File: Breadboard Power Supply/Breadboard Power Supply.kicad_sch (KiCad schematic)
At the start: 17 parts, among them J1 Conn_01x02_Pin, J2 Conn_01x02_Pin, J3 Conn_01x03_Pin, J4 Conn_01x03_Pin, J5 Screw_Terminal_01x02, J6 Screw_Terminal_01x02, J7 Barrel_Jack_Switch, U1 LM7805_TO220, U2 LM317_TO-220

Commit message: Add power input/output net classes and update schematic labels for clarity
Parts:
- D1: Purpose (none) -> Power
- J1, J2: Purpose (none) -> Output to breadboard
- J3: Purpose (none) -> Output voltage selector 1
- J4: Purpose (none) -> Output voltage selector 2
- J5, J6: Purpose (none) -> Output to jumper wires
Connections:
- net PWR_output: now reaches J1.2 (Pin_2), J3.2 (Pin_2), J5.2 (Pin_2)
- net PWR_output: now also J2.2 (Pin_2), J4.2 (Pin_2), J6.2 (Pin_2)
- net PWR_input: now reaches J7.1, S1.2
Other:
- note added: "3.3V circuit"
- note added: "GND (Pin 1)"
- note added: "Input and 5V circuit"
- note added: "Output and switches"
- moved on the sheet: J3, J4
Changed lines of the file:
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@@
 		(rev "1")
+	)
+	(rectangle
+		(start 40.64 91.44)
+		(end 151.13 145.415)
+		(stroke
+			(width 0)
+			(type default)
+		)
+		(fill
+			(type none)
+		)
+	)
+	(rectangle
+		(start 179.705 47.625)
+		(end 244.475 155.575)
+		(stroke
+			(width 0)
+			(type default)
+		)
+		(fill
+			(type none)
+		)
+	)
+	(rectangle
+		(start 26.035 27.305)
+		(end 151.13 78.74)
+		(stroke
+			(width 0)
+			(type default)
+		)
+		(fill
+			(type none)
+		)
+	)
+	(text "3.3V circuit"
+		(exclude_from_sim no)
+		(at 46.99 88.9 0)
+		(effects
+			(font
+				(size 1.27 1.27)
+			)
+		)
+	)
+	(text "GND (Pin 1)"
+		(exclude_from_sim no)
+		(at 210.82 137.16 0)
+		(effects
+			(font
+				(size 1.27 1.27)
+			)
+		)
+	)
+	(text "Output and switches"
+		(exclude_from_sim no)
+		(at 189.23 44.45 0)
+		(effects
+			(font
+				(size 1.27 1.27)
+			)
+		)
+	)
+	(text "GND (Pin 1)"
+		(exclude_from_sim no)
+		(at 210.82 81.28 0)
+		(effects
+			(font
+				(size 1.27 1.27)
+			)
+		)
+	)
+	(text "Input and 5V circuit"
+		(exclude_from_sim no)
+		(at 35.56 25.4 0)
+		(effects
+			(font
+				(size 1.27 1.27)
+			)
+		)
 	)
 	(junction
@@
 	(wire
 		(pts
-			(xy 201.93 60.96) (xy 201.93 68.58)
+			(xy 201.93 58.42) (xy 201.93 68.58)
 		)
 		(stroke
@@
 	(wire
 		(pts
-			(xy 208.28 116.84) (xy 201.93 116.84)
+			(xy 208.28 114.3) (xy 201.93 114.3)
 		)
 		(stroke
@@
 	(wire
 		(pts
-			(xy 208.28 60.96) (xy 201.93 60.96)
+			(xy 208.28 58.42) (xy 201.93 58.42)
 		)
 		(stroke
@@
 	(wire
 		(pts
-			(xy 201.93 116.84) (xy 201.93 124.46)
+			(xy 201.93 114.3) (xy 201.93 124.46)
 		)
 		(stroke
@@
 		)
 	)
+	(label "PWR_output"
+		(at 201.93 121.92 180)
+		(effects
+			(font
+				(size 1.27 1.27)
+			)
+			(justify right bottom)
+		)
+	)
 	(label "12V"
 		(at 57.15 101.6 0)
@@
 	)
 	(label "5V"
-		(at 208.28 58.42 180)
+		(at 208.28 55.88 180)
 		(effects
 			(font
@@
 		)
 	)
+	(label "PWR_output"
+		(at 201.93 66.04 180)
+		(effects
+			(font
+				(size 1.27 1.27)
+			)
+			(justify right bottom)
+		)
+	)
 	(label "3.3V"
-		(at 208.28 63.5 180)
+		(at 208.28 60.96 180)
 		(effects
 			(font
@@
 	)
 	(label "5V"
-		(at 208.28 114.3 180)
+		(at 208.28 111.76 180)
 		(effects
 			(font
@@
 		)
 	)
+	(label "PWR_input"
+		(at 53.34 45.72 0)
+		(effects
+			(font
+				(size 1.27 1.27)
+			)
+			(justify left bottom)
+		)
+	)
 	(label "3.3V"
-		(at 208.28 119.38 180)
+		(at 208.28 116.84 180)
 		(effects
 			(font
@@
 		)
 		(property "Value" "Screw_Terminal_01x02"
-			(at 213.36 76.2001 0)
+			(at 203.2 73.66 0)
 			(effects
 				(font
@@
 				)
 				(hide yes)
+			)
+		)
+		(property "Purpose" "Output to jumper wires"
+			(at 224.79 76.2 0)
+			(effects
+				(font
+					(size 1.27 1.27)
+				)
 			)
 		)
@@
 		(on_board yes)
 		(dnp no)
-		(fields_autoplaced yes)
 		(property "Reference" "J2"
 			(at 214.63 124.4599 0)
@@
 				)
 				(hide yes)
+			)
+		)
+		(property "Purpose" "Output to breadboard"
+			(at 213.36 121.92 0)
+			(effects
+				(font
+					(size 1.27 1.27)
+				)
 			)
 		)
@@
 		(on_board yes)
 		(dnp no)
-		(fields_autoplaced yes)
 		(property "Reference" "J1"
 			(at 214.63 68.5799 0)
@@
 				)
 				(hide yes)
+			)
+		)
+		(property "Purpose" "Output to breadboard"
+			(at 213.36 66.04 0)
+			(effects
+				(font
+					(size 1.27 1.27)
+				)
 			)
 		)
@@
 	(symbol
 		(lib_id "Connector:Conn_01x03_Pin")
-		(at 213.36 60.96 180)
+		(at 213.36 58.42 180)
 		(unit 1)
 		(exclude_from_sim no)
@@
 		(on_board yes)
 		(dnp no)
-		(fields_autoplaced yes)
 		(property "Reference" "J3"
+			(at 214.63 57.1499 0)
+			(effects
+				(font
+					(size 1.27 1.27)
+				)
+				(justify right)
+			)
+		)
+		(property "Value" "Conn_01x03_Pin"
 			(at 214.63 59.6899 0)
 			(effects
@@
 			)
 		)
-		(property "Value" "Conn_01x03_Pin"
-			(at 214.63 62.2299 0)
-			(effects
-				(font
-					(size 1.27 1.27)
-				)
-				(justify right)
-			)
-		)
 		(property "Footprint" "Connector_PinHeader_2.54mm:PinHeader_1x03_P2.54mm_Vertical"
-			(at 213.36 60.96 0)
+			(at 213.36 58.42 0)
 			(effects
 				(font
@@
 		)
 		(property "Datasheet" "~"
-			(at 213.36 60.96 0)
+			(at 213.36 58.42 0)
 			(effects
 				(font
@@
 		)
 		(property "Description" "Generic connector, single row, 01x03, script generated"
-			(at 213.36 60.96 0)
-			(effects
-				(font
-					(size 1.27 1.27)
-				)
-				(hide yes)
+			(at 213.36 58.42 0)
+			(effects
+				(font
+					(size 1.27 1.27)
+				)
+				(hide yes)
+			)
+		)
+		(property "Purpose" "Output voltage selector 1"
+			(at 213.36 52.07 0)
+			(effects
+				(font
+					(size 1.27 1.27)
+				)
 			)
 		)
@@
 	(symbol
 		(lib_id "Connector:Conn_01x03_Pin")
-		(at 213.36 116.84 180)
+		(at 213.36 114.3 180)
 		(unit 1)
 		(exclude_from_sim no)
@@
 		(on_board yes)
 		(dnp no)
-		(fields_autoplaced yes)
 		(property "Reference" "J4"
+			(at 214.63 113.0299 0)
+			(effects
+				(font
+					(size 1.27 1.27)
+				)
+				(justify right)
+			)
+		)
+		(property "Value" "Conn_01x03_Pin"
 			(at 214.63 115.5699 0)
 			(effects
@@
 			)
 		)
-		(property "Value" "Conn_01x03_Pin"
-			(at 214.63 118.1099 0)
-			(effects
-				(font
-					(size 1.27 1.27)
-				)
-				(justify right)
-			)
-		)
 		(property "Footprint" "Connector_PinHeader_2.54mm:PinHeader_1x03_P2.54mm_Vertical"
-			(at 213.36 116.84 0)
+			(at 213.36 114.3 0)
 			(effects
 				(font
@@
 		)
 		(property "Datasheet" "~"
-			(at 213.36 116.84 0)
+			(at 213.36 114.3 0)
 			(effects
 				(font
@@
 		)
 		(property "Description" "Generic connector, single row, 01x03, script generated"
-			(at 213.36 116.84 0)
-			(effects
-				(font
-					(size 1.27 1.27)
-				)
-				(hide yes)
+			(at 213.36 114.3 0)
+			(effects
+				(font
+					(size 1.27 1.27)
+				)
+				(hide yes)
+			)
+		)
+		(property "Purpose" "Output voltage selector 2"
+			(at 213.36 107.95 0)
+			(effects
+				(font
+					(size 1.27 1.27)
+				)
 			)
 		)
@@
 		)
 		(property "Value" "Screw_Terminal_01x02"
-			(at 213.36 132.0801 0)
+			(at 203.2 129.54 0)
 			(effects
 				(font
@@
 				)
 				(hide yes)
+			)
+		)
+		(property "Purpose" "Output to jumper wires"
+			(at 224.79 132.08 0)
+			(effects
+				(font
+					(size 1.27 1.27)
+				)
 			)
 		)
@@
 		(on_board yes)
 		(dnp no)
-		(fields_autoplaced yes)
 		(property "Reference" "D1"
 			(at 77.7875 127 0)
@@
 			)
 		)
+		(property "Purpose" "Power"
+			(at 76.2 137.16 0)
+			(effects
+				(font
+					(size 1.27 1.27)
+				)
+			)
+		)

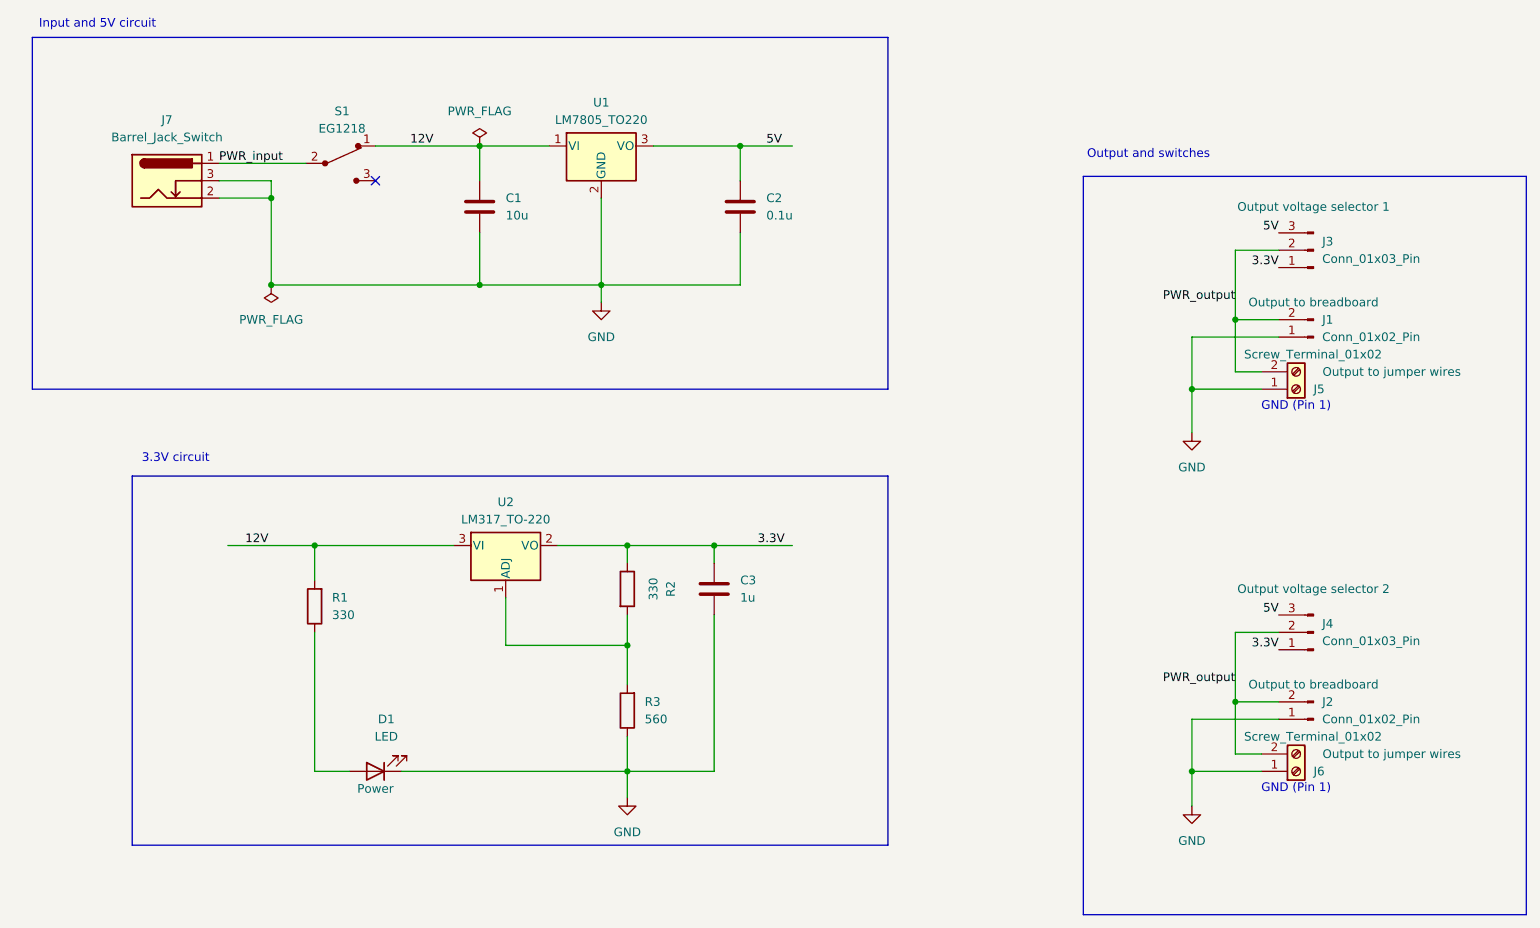
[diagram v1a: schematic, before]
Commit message: Update schematic labels for consistency and enhance design settings in KiCad project
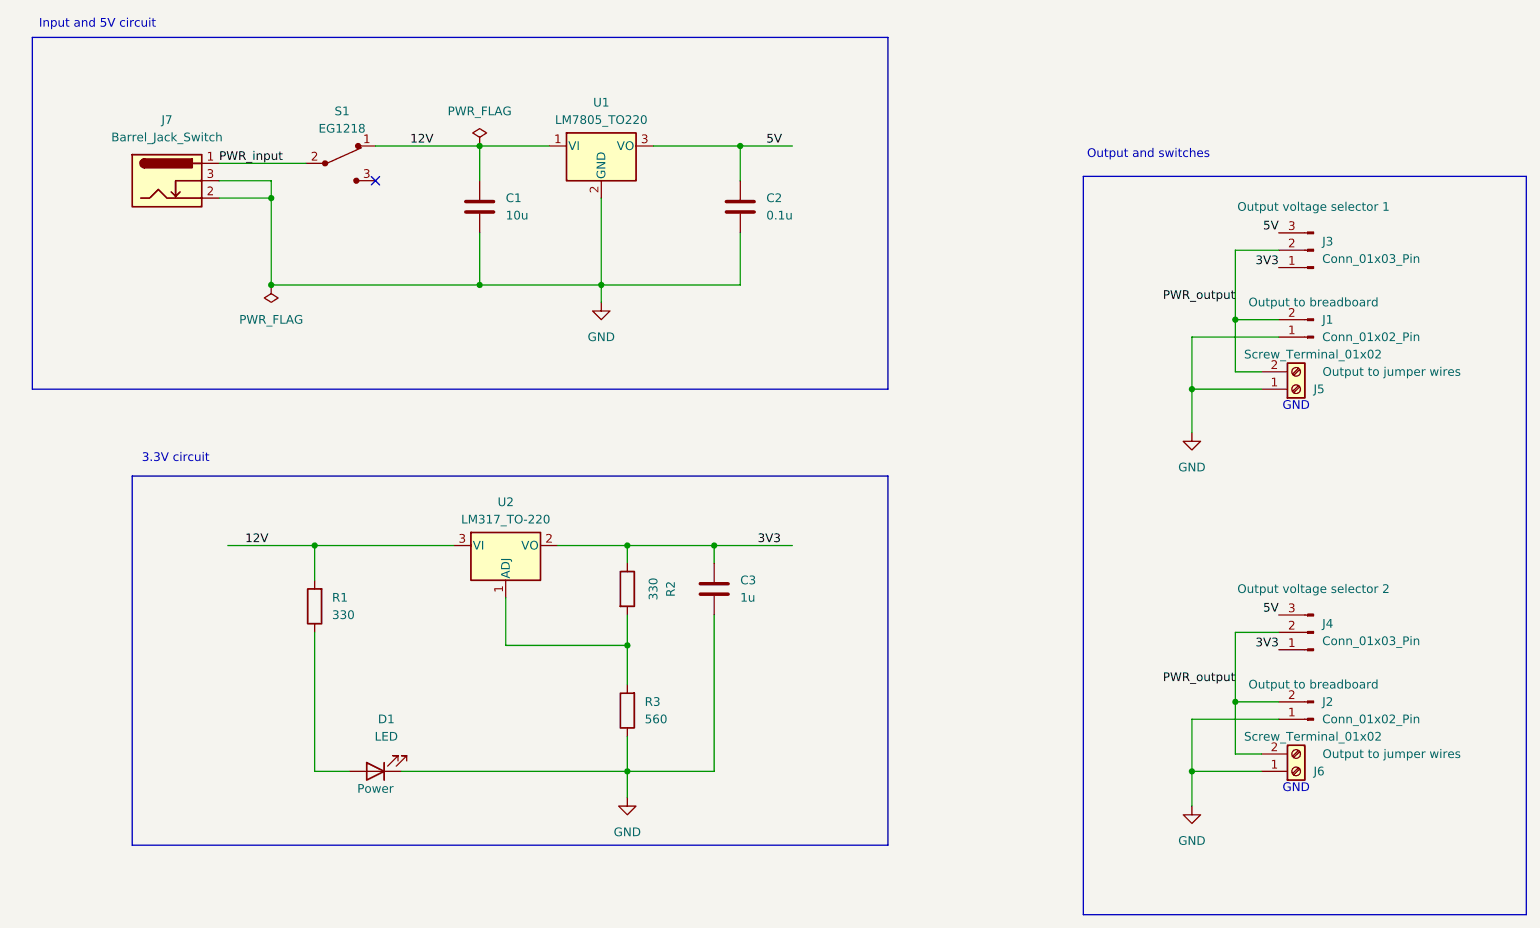
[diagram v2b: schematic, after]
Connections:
- net 3.3V renamed 3V3
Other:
- note added: "GND"
- note removed: "GND (Pin 1)"
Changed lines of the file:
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@@
 		)
 	)
-	(text "GND (Pin 1)"
+	(text "GND"
 		(exclude_from_sim no)
 		(at 210.82 137.16 0)
@@
 		)
 	)
-	(text "GND (Pin 1)"
+	(text "GND"
 		(exclude_from_sim no)
 		(at 210.82 81.28 0)
@@
 		)
 	)
-	(label "3.3V"
+	(label "3V3"
 		(at 132.08 101.6 0)
 		(effects
@@
 		)
 	)
-	(label "3.3V"
+	(label "3V3"
 		(at 208.28 60.96 180)
 		(effects
@@
 		)
 	)
-	(label "3.3V"
+	(label "3V3"
 		(at 208.28 116.84 180)
 		(effects
